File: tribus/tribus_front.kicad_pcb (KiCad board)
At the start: 2 copper layers, 30 x 106 mm, 46 parts, among them J10 SNARE_TRIG, J11 Conn_01x08_Male, J2 HIHAT_TRIG, J3 SNARE_MIX_OUT, J5 BASS_OUT, J6 HH_OUT, J8 BASS_TRIG, J9 Conn_01x08_Female, U4 TL074

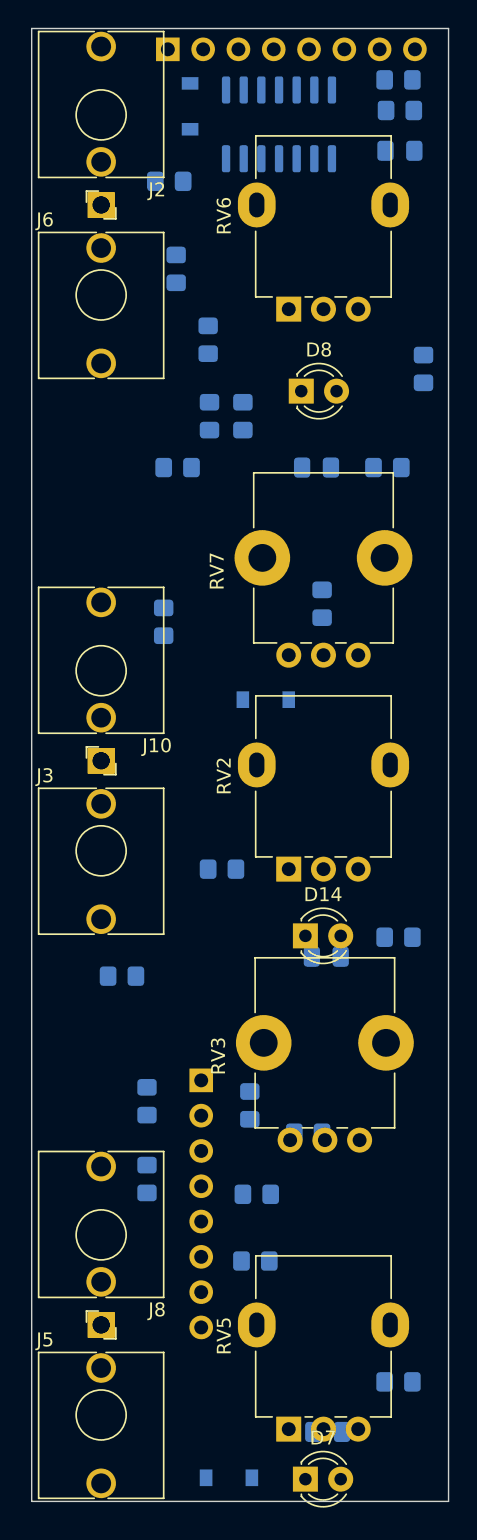
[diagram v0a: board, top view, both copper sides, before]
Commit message: Fix wrong resistor value, add routes
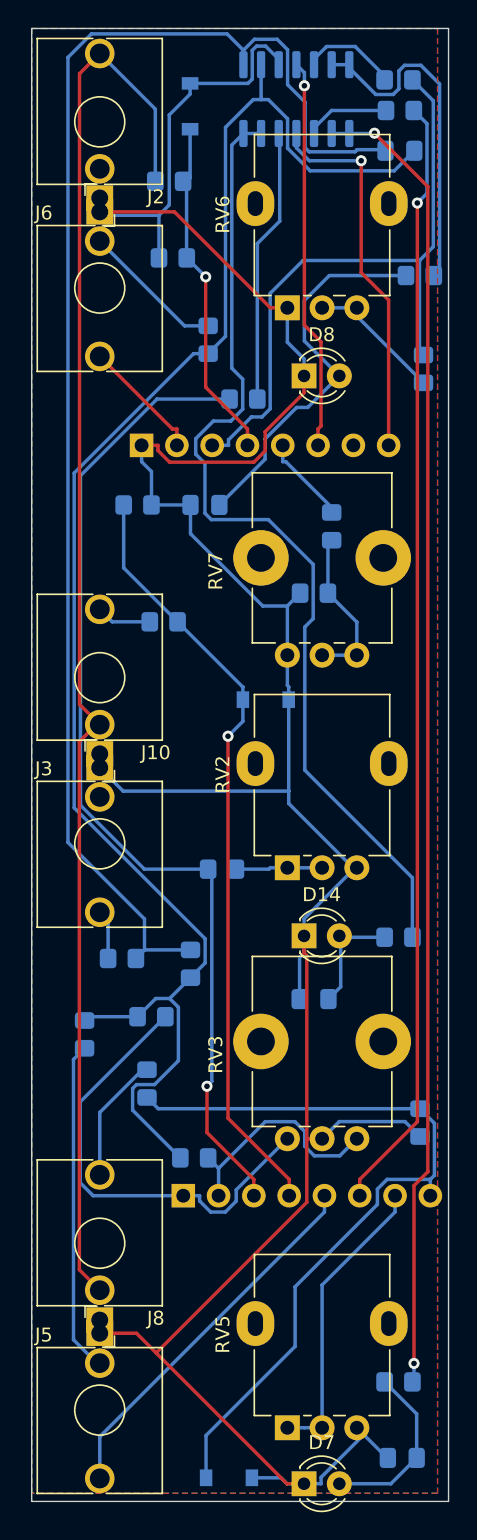
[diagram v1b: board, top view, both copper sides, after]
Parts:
- moved J11 29.3 mm to (16.8, 30.0)
- moved R56 21.9 mm to (11.4, 67.3), turned to 90 degrees
- moved R61 14.0 mm to (27.9, 17.8)
- moved R69 11.8 mm to (21.6, 35.8)
- moved R17 11.3 mm to (3.81, 72.4)
- moved J9 11.3 mm to (19.8, 84.0), turned to 270 degrees
- moved R26 9.53 mm to (8.62, 71.1), turned to 180 degrees
- moved C39 8.47 mm to (12.5, 34.3)
- moved R65 8.08 mm to (27.9, 78.7), turned to 270 degrees
- moved RV3 8.07 mm to (20.9, 72.4)
- moved RV2 7.97 mm to (20.9, 52.9)
- moved RV6 7.97 mm to (20.9, 12.6)
- moved RV5 7.97 mm to (20.9, 93.2)
- moved RV7 7.94 mm to (20.9, 37.6)
- moved J5 6.10 mm to (4.90, 99.4)
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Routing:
- net GND: track 0.00 -> 210.9 mm
- net Net-(C21-Pad2): track 0.00 -> 115.7 mm
- net Net-(C21-Pad1): track 0.00 -> 102.9 mm
- net INPUT_NORM: track 0.00 -> 102.4 mm
- net Net-(R29-Pad2): track 0.00 -> 95.0 mm, vias 0 -> 2
- net BASS_LED_FRONT: track 0.00 -> 80.5 mm, vias 0 -> 1
- net SNARE_DECAY_FRONT: track 0.00 -> 73.0 mm, vias 0 -> 1
- net Net-(R63-Pad2): track 0.00 -> 71.3 mm
- net BASS_TRIG_FRONT: track 0.00 -> 56.8 mm
- net SNARE_TRIGGER_FRONT: track 0.00 -> 55.5 mm, vias 0 -> 1
- net HH_DECAY_FRONT: track 0.00 -> 46.5 mm
- net SNARE_BODY_FRONT: track 0.00 -> 33.1 mm
- net -12V: track 0.00 -> 28.2 mm, vias 0 -> 1
- net Net-(C39-Pad2): track 0.00 -> 27.9 mm
- net +12V: track 0.00 -> 27.4 mm, vias 0 -> 1
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- added copper zone on B.Cu, net (none)
- added copper zone on F.Cu, net (none)

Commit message: Make ELFO nicer, fix issues
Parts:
- added REF**: OSHW-Logo_7.5x8mm_SilkScreen, Symbol:OSHW-Logo_7.5x8mm_SilkScreen, B.Cu at (20.9, 95.2)
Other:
- board text added: "PCB by Pedro Ferreira Licensed under CERN-OHL-P v2"
- board text added: "T r i b u s"
- board text added: "https://bit.ly/2OCx7gC"

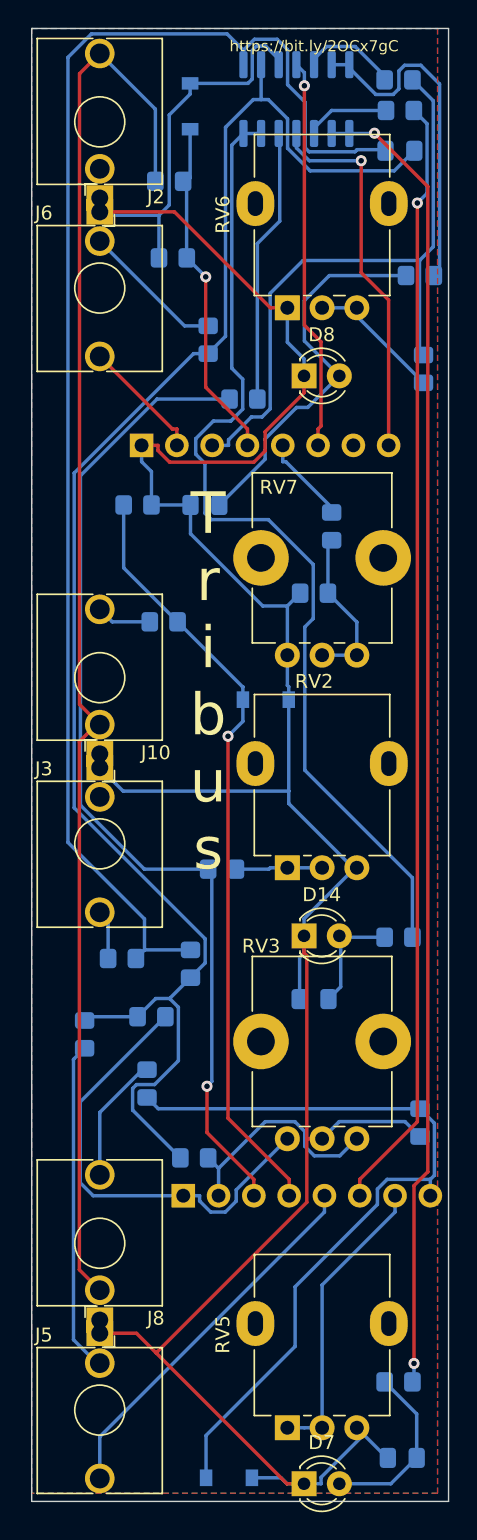
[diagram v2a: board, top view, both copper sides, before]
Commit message: Use 1206 resistors, because I messed up :facepalm:
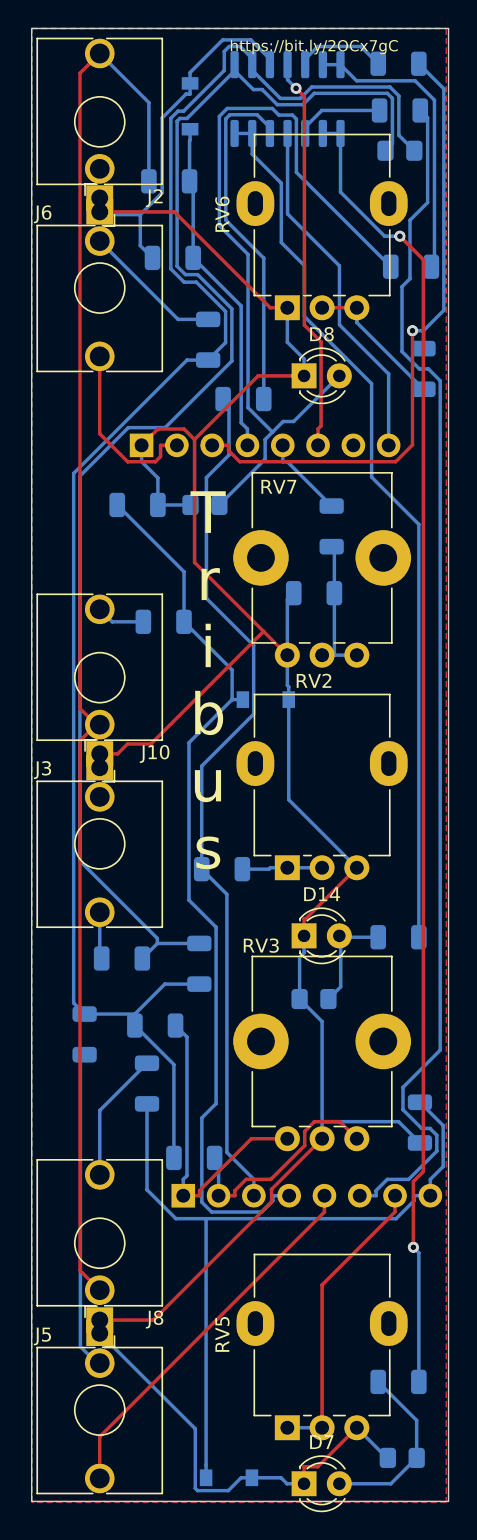
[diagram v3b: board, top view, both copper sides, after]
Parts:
- R13, R15, R16, R17, R20, R26, R29, R56, R57, R59, R60, R61, R62, R63, R64, R65, R66, R67, R68, R69, R7, R8: footprint Resistor_SMD:R_0805_2012Metric_Pad1.20x1.40mm_HandSolder -> Resistor_SMD:R_1206_3216Metric
- moved R59 1.16 mm to (26.4, 2.54)
- moved R61 0.90 mm to (27.3, 17.1)
- moved REF** 0.87 mm to (20.3, 94.6)
- moved R26 0.69 mm to (8.89, 71.8)
- moved U4 0.64 mm to (18.4, 5.08)
- moved R56 0.63 mm to (12.1, 67.3)
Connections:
- J11 pad 7: (no net) -> Net-(J11-Pad7)
- J2 pad TN: (no net) -> Net-(J2-PadTN)
- J3 pad TN: (no net) -> Net-(J3-PadTN)
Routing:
- net Net-(C39-Pad2): track 27.9 -> 57.2 mm
- net SNARE_BODY_FRONT: track 33.1 -> 22.1 mm
- net SNARE_DECAY_FRONT: track 73.0 -> 62.7 mm, vias 1 -> 0
- net SNARE_TRIGGER_FRONT: track 55.5 -> 64.2 mm, vias 1 -> 0
- net Net-(R63-Pad2): track 71.3 -> 64.1 mm
- net BASS_LED_FRONT: track 80.5 -> 87.0 mm, vias 1 -> 0
- net Net-(C21-Pad1): track 102.9 -> 97.2 mm
- net Net-(R62-Pad1): track 19.8 -> 25.4 mm
- net HH_OUT_FRONT: track 8.89 -> 12.9 mm
- net Net-(R61-Pad2): track 24.9 -> 21.2 mm
- net Net-(C21-Pad2): track 115.7 -> 119.4 mm
- net BASS_TRIG_FRONT: track 56.8 -> 54.8 mm
- net +12V: track 27.4 -> 25.5 mm, vias 1 -> 0
- net Net-(R67-Pad2): track 11.7 -> 10.4 mm
- net BASS_OUT_MIX: track 23.9 -> 23.0 mm
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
